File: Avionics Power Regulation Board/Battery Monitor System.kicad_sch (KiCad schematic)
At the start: 36 parts, among them Q1 NMOS, Q2 NMOS, Q3 NMOS, SW1 SW_Push, U2 BQ76920PW

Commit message: Updated Subscale Board
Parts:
- R3, R4, R5, R6, R7, R8, R9, RC1, RC2, RC3, RC4, RC5, RF1, RSNS1: footprint MFR_25FRF52_10K:RESAD1100W55L680D260 -> Resistor_SMD:R_0805_2012Metric_Pad1.20x1.40mm_HandSolder
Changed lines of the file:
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@@
 			)
 		)
-		(property "Footprint" "MFR_25FRF52_10K:RESAD1100W55L680D260"
+		(property "Footprint" "Resistor_SMD:R_0805_2012Metric_Pad1.20x1.40mm_HandSolder"
 			(at 81.534 86.614 90)
 			(effects
@@
 			)
 		)
-		(property "Footprint" "MFR_25FRF52_10K:RESAD1100W55L680D260"
+		(property "Footprint" "Resistor_SMD:R_0805_2012Metric_Pad1.20x1.40mm_HandSolder"
 			(at 81.534 37.084 90)
 			(effects
@@
 			)
 		)
-		(property "Footprint" "MFR_25FRF52_10K:RESAD1100W55L680D260"
+		(property "Footprint" "Resistor_SMD:R_0805_2012Metric_Pad1.20x1.40mm_HandSolder"
 			(at 112.014 53.594 90)
 			(effects
@@
 			)
 		)
-		(property "Footprint" "MFR_25FRF52_10K:RESAD1100W55L680D260"
+		(property "Footprint" "Resistor_SMD:R_0805_2012Metric_Pad1.20x1.40mm_HandSolder"
 			(at 82.296 127.254 90)
 			(effects
@@
 			)
 		)
-		(property "Footprint" "MFR_25FRF52_10K:RESAD1100W55L680D260"
+		(property "Footprint" "Resistor_SMD:R_0805_2012Metric_Pad1.20x1.40mm_HandSolder"
 			(at 118.364 133.096 90)
 			(effects
@@
 			)
 		)
-		(property "Footprint" "MFR_25FRF52_10K:RESAD1100W55L680D260"
+		(property "Footprint" "Resistor_SMD:R_0805_2012Metric_Pad1.20x1.40mm_HandSolder"
 			(at 67.056 127.254 90)
 			(effects
@@
 			)
 		)
-		(property "Footprint" "MFR_25FRF52_10K:RESAD1100W55L680D260"
+		(property "Footprint" "Resistor_SMD:R_0805_2012Metric_Pad1.20x1.40mm_HandSolder"
 			(at 192.024 35.306 90)
 			(effects
@@
 			)
 		)
-		(property "Footprint" "MFR_25FRF52_10K:RESAD1100W55L680D260"
+		(property "Footprint" "Resistor_SMD:R_0805_2012Metric_Pad1.20x1.40mm_HandSolder"
 			(at 153.924 133.096 90)
 			(effects
@@
 			)
 		)
-		(property "Footprint" "MFR_25FRF52_10K:RESAD1100W55L680D260"
+		(property "Footprint" "Resistor_SMD:R_0805_2012Metric_Pad1.20x1.40mm_HandSolder"
 			(at 81.534 25.654 90)
 			(effects
@@
 			)
 		)
-		(property "Footprint" "MFR_25FRF52_10K:RESAD1100W55L680D260"
+		(property "Footprint" "Resistor_SMD:R_0805_2012Metric_Pad1.20x1.40mm_HandSolder"
 			(at 165.354 106.426 90)
 			(effects
@@
 			)
 		)
-		(property "Footprint" "MFR_25FRF52_10K:RESAD1100W55L680D260"
+		(property "Footprint" "Resistor_SMD:R_0805_2012Metric_Pad1.20x1.40mm_HandSolder"
 			(at 81.534 48.514 90)
 			(effects
@@
 			)
 		)
-		(property "Footprint" "MFR_25FRF52_10K:RESAD1100W55L680D260"
+		(property "Footprint" "Resistor_SMD:R_0805_2012Metric_Pad1.20x1.40mm_HandSolder"
 			(at 119.634 60.706 90)
 			(effects
@@
 			)
 		)
-		(property "Footprint" "MFR_25FRF52_10K:RESAD1100W55L680D260"
+		(property "Footprint" "Resistor_SMD:R_0805_2012Metric_Pad1.20x1.40mm_HandSolder"
 			(at 73.914 138.684 90)
 			(effects
@@
 			)
 		)
-		(property "Footprint" "MFR_25FRF52_10K:RESAD1100W55L680D260"
+		(property "Footprint" "Resistor_SMD:R_0805_2012Metric_Pad1.20x1.40mm_HandSolder"
 			(at 81.534 59.944 90)
 			(effects

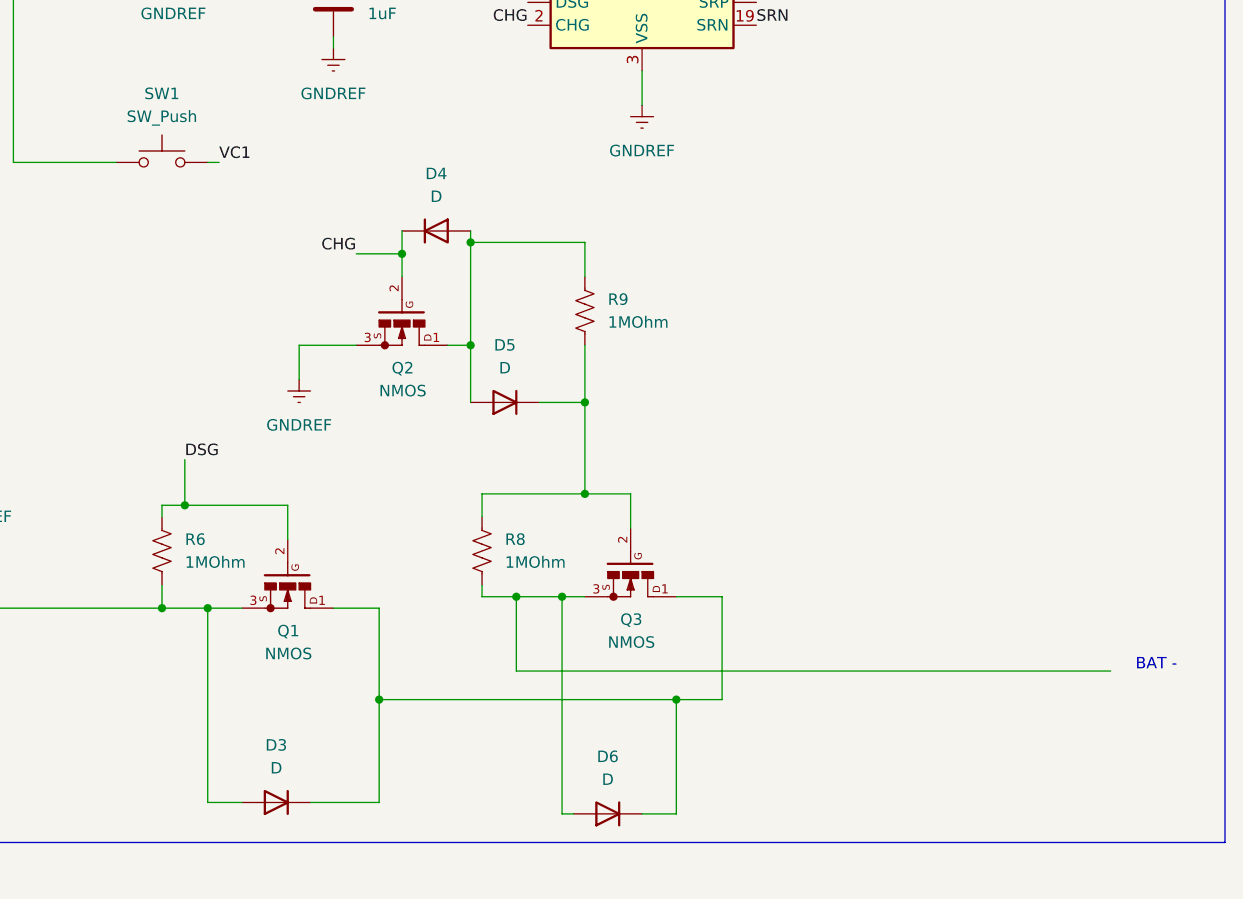
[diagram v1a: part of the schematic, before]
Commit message: Fixed PMOS
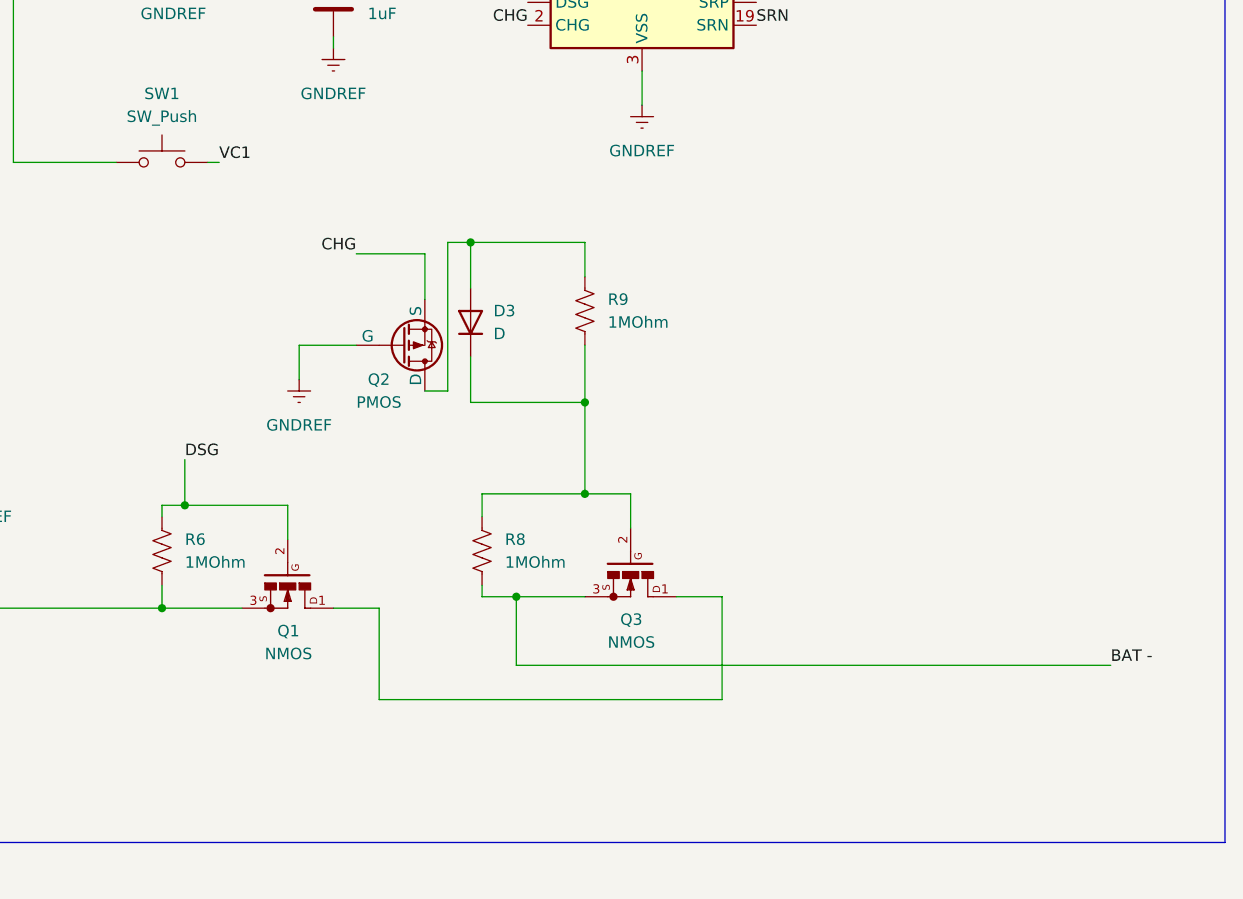
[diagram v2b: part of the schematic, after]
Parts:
- removed D4, D5, D6: D, Diode_THT:D_DO-41_SOD81_P10.16mm_Horizontal, symbol Diode:1N4007
- removed Q2: NMOS, BS170:TO92, symbol BS170:BS170
- added Q2: PMOS, BS170:TO92, symbol Simulation_SPICE:PMOS
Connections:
- net CHG: now also Q2.3 (S)
- net GNDREF: now also Q2.2 (G)
- net at R9.2: now also D3.2 (A), Q2.1 (D)
- net at Q1.3, R4.2, R6.1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: no longer D3.2 (A)
- net at Q1.1, Q3.1: no longer D3.1 (K)
- net BAT -: now reaches Q3.3, R8.1
- net at Q3.2, R8.2, R9.1: now also D3.1 (K)
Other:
- note removed: "BAT -"

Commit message: Step Files
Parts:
- Q1, Q2, Q3: footprint BS170:TO92 -> BS170_2:TO92
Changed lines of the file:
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@@
 			)
 		)
-		(property "Footprint" "BS170:TO92"
+		(property "Footprint" "BS170_2:TO92"
 			(at 171.45 135.89 0)
 			(effects
@@
 				(justify bottom)
 				(hide yes)
+			)
+		)
+		(property "Purpose" ""
+			(at 171.45 135.89 0)
+			(effects
+				(font
+					(size 1.27 1.27)
+				)
 			)
 		)
@@
 			)
 		)
-		(property "Footprint" "BS170:TO92"
+		(property "Footprint" "BS170_2:TO92"
 			(at 133.35 137.16 0)
 			(effects
@@
 				(justify bottom)
 				(hide yes)
+			)
+		)
+		(property "Purpose" ""
+			(at 133.35 137.16 0)
+			(effects
+				(font
+					(size 1.27 1.27)
+				)
 			)
 		)
@@
 			)
 		)
-		(property "Footprint" "BS170:TO92"
+		(property "Footprint" "BS170_2:TO92"
 			(at 151.13 113.03 0)
 			(effects

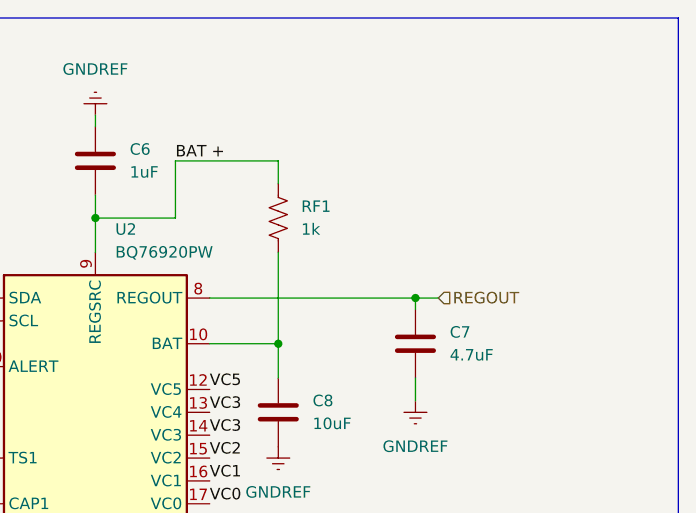
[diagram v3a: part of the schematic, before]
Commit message: Removed one of the transformer
Must Redo the traces when you get home
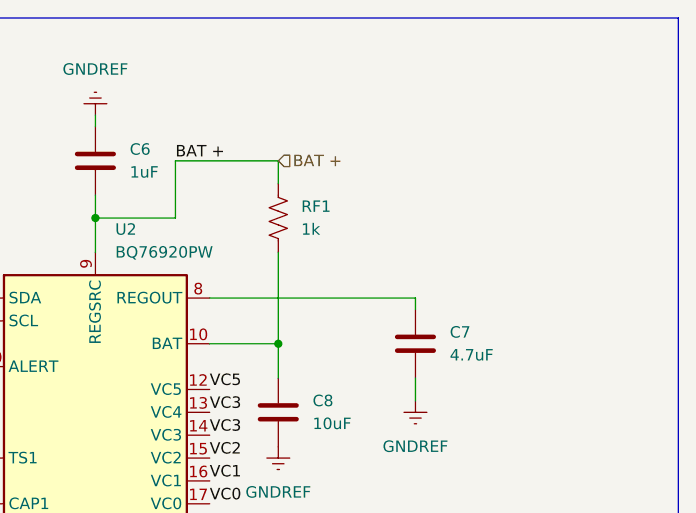
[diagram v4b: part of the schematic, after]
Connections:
- net REGOUT: no longer names the net of C7.2, U2.8 (REGOUT)
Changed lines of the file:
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@@
-	)
-	(junction
-		(at 208.28 44.45)
-		(diameter 0)
-		(color 0 0 0 0)
 	)
 	(junction
@@
 		(pts
 			(xy 92.71 118.11) (xy 99.06 118.11)
-		)
-		(stroke
-			(width 0)
-			(type default)
-		)
-	)
-	(wire
-		(pts
-			(xy 208.28 44.45) (xy 210.82 44.45)
 		)
 		(stroke
@@
 		)
 	)
-	(hierarchical_label "REGOUT"
+	(hierarchical_label "BAT +"
 		(shape input)
-		(at 210.82 44.45 0)
-		(fields_autoplaced yes)
-		(effects
+		(at 193.04 29.21 0)
+		(fields_autoplaced yes)
+		(effects
